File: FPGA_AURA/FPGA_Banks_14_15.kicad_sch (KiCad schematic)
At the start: 15 parts, among them U1 XC7A35T-2FTG256C

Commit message: DDR3 Routing closed!
Finally DDR3 has been routed, verified, and length matched. Further validation still required.
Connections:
- net DDR3_A0: now also U1.D10 (IO_0_15); no longer U1.B11 (IO_L4N_T0_15)
- net DDR3_A1: now also U1.C14 (IO_L8P_T1_AD10P_15); no longer U1.B16 (IO_L10N_T1_AD11N_15)
- net DDR3_A10: now also U1.C12 (IO_L11N_T1_SRCC_15); no longer U1.A14 (IO_L7N_T1_AD2N_15)
- net DDR3_A12: now also U1.C13 (IO_L12N_T1_MRCC_15); no longer U1.A15 (IO_L9N_T1_DQS_AD3N_15)
- net DDR3_A13: now also U1.B10 (IO_L4P_T0_15); no longer U1.D10 (IO_0_15)
- net DDR3_A2: now also U1.D13 (IO_L12P_T1_MRCC_15); no longer U1.C13 (IO_L12N_T1_MRCC_15)
- net DDR3_A3: now also U1.A15 (IO_L9N_T1_DQS_AD3N_15); no longer U1.B12 (IO_L5P_T0_AD9P_15)
- net DDR3_A4: now also U1.A12 (IO_L5N_T0_AD9N_15); no longer U1.B10 (IO_L4P_T0_15)
- net DDR3_A5: now also U1.B15 (IO_L9P_T1_DQS_AD3P_15); no longer U1.D8 (IO_L6P_T0_15)
- net DDR3_A6: now also U1.B11 (IO_L4N_T0_15); no longer U1.C9 (IO_L1N_T0_AD0N_15)
- net DDR3_A7: now also U1.B16 (IO_L10N_T1_AD11N_15); no longer U1.C8 (IO_L1P_T0_AD0P_15)
- net DDR3_A9: now also U1.C16 (IO_L10P_T1_AD11P_15); no longer U1.D9 (IO_L6N_T0_VREF_15)
- net DDR3_BA0: now also U1.B14 (IO_L8N_T1_AD10N_15); no longer U1.C12 (IO_L11N_T1_SRCC_15)
- net DDR3_BA1: now also U1.B12 (IO_L5P_T0_AD9P_15); no longer U1.A12 (IO_L5N_T0_AD9N_15)
- net DDR3_BA2: now also U1.D9 (IO_L6N_T0_VREF_15); no longer U1.A13 (IO_L7P_T1_AD2P_15)
- net DDR3_CAS: now also U1.A13 (IO_L7P_T1_AD2P_15); no longer U1.B14 (IO_L8N_T1_AD10N_15)
- net DDR3_CS: now also U1.A14 (IO_L7N_T1_AD2N_15); no longer U1.B15 (IO_L9P_T1_DQS_AD3P_15)
- net DDR3_ODT: now also U1.C8 (IO_L1P_T0_AD0P_15); no longer U1.C16 (IO_L10P_T1_AD11P_15)
- net DDR3_RAS: now also U1.D8 (IO_L6P_T0_15); no longer U1.C14 (IO_L8P_T1_AD10P_15)
- net DDR3_WE: now also U1.C9 (IO_L1N_T0_AD0N_15); no longer U1.D13 (IO_L12P_T1_MRCC_15)

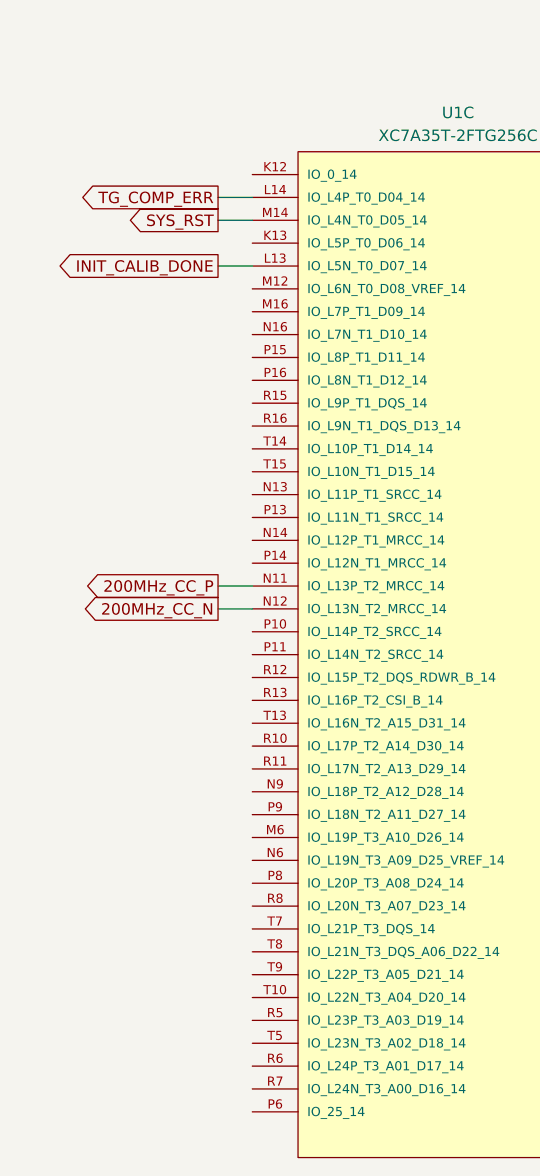
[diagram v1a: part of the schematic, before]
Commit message: Started pinout after successful Vivado bitstream generation.
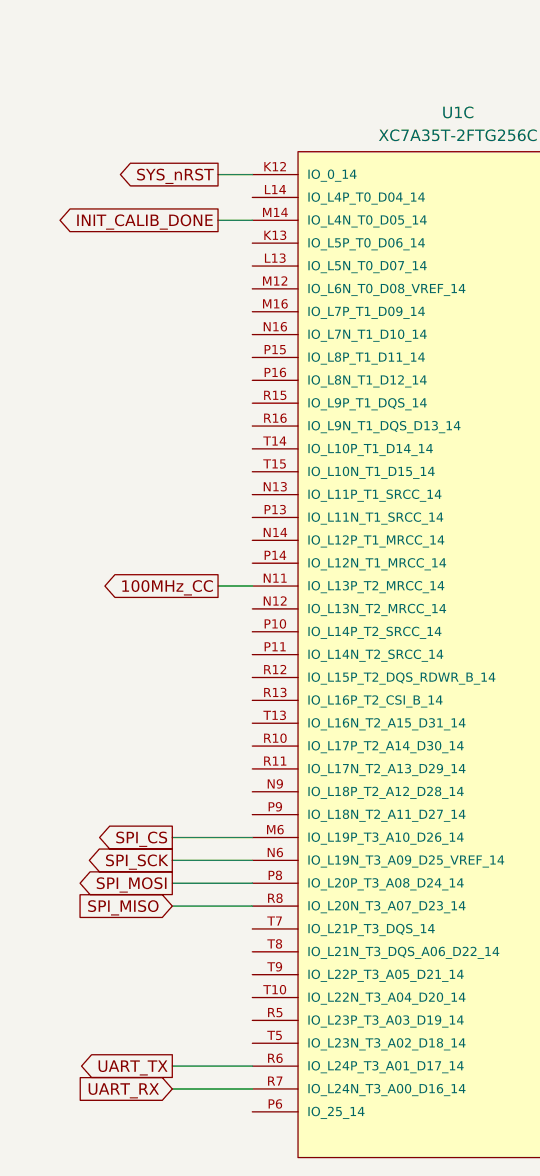
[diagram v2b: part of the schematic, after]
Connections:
- net SYS_RST is gone; now on net INIT_CALIB_DONE: U1.M14 (IO_L4N_T0_D05_14)
- net INIT_CALIB_DONE: no longer U1.L13 (IO_L5N_T0_D07_14)
- net SYS_nRST: now reaches U1.K12 (IO_0_14)
- net SPI_CS: now reaches U1.M6 (IO_L19P_T3_A10_D26_14)
- net SPI_SCK: now reaches U1.N6 (IO_L19N_T3_A09_D25_VREF_14)
- net SPI_MOSI: now reaches U1.P8 (IO_L20P_T3_A08_D24_14)
- net UART_TX: now reaches U1.R6 (IO_L24P_T3_A01_D17_14)
- net UART_RX: now reaches U1.R7 (IO_L24N_T3_A00_D16_14)
- net SPI_MISO: now reaches U1.R8 (IO_L20N_T3_A07_D23_14)
- net 200MHz_CC_N: no longer names the net of U1.N12 (IO_L13N_T2_MRCC_14)
- net 200MHz_CC_P renamed 100MHz_CC
- net TG_COMP_ERR: no longer names the net of U1.L14 (IO_L4P_T0_D04_14)

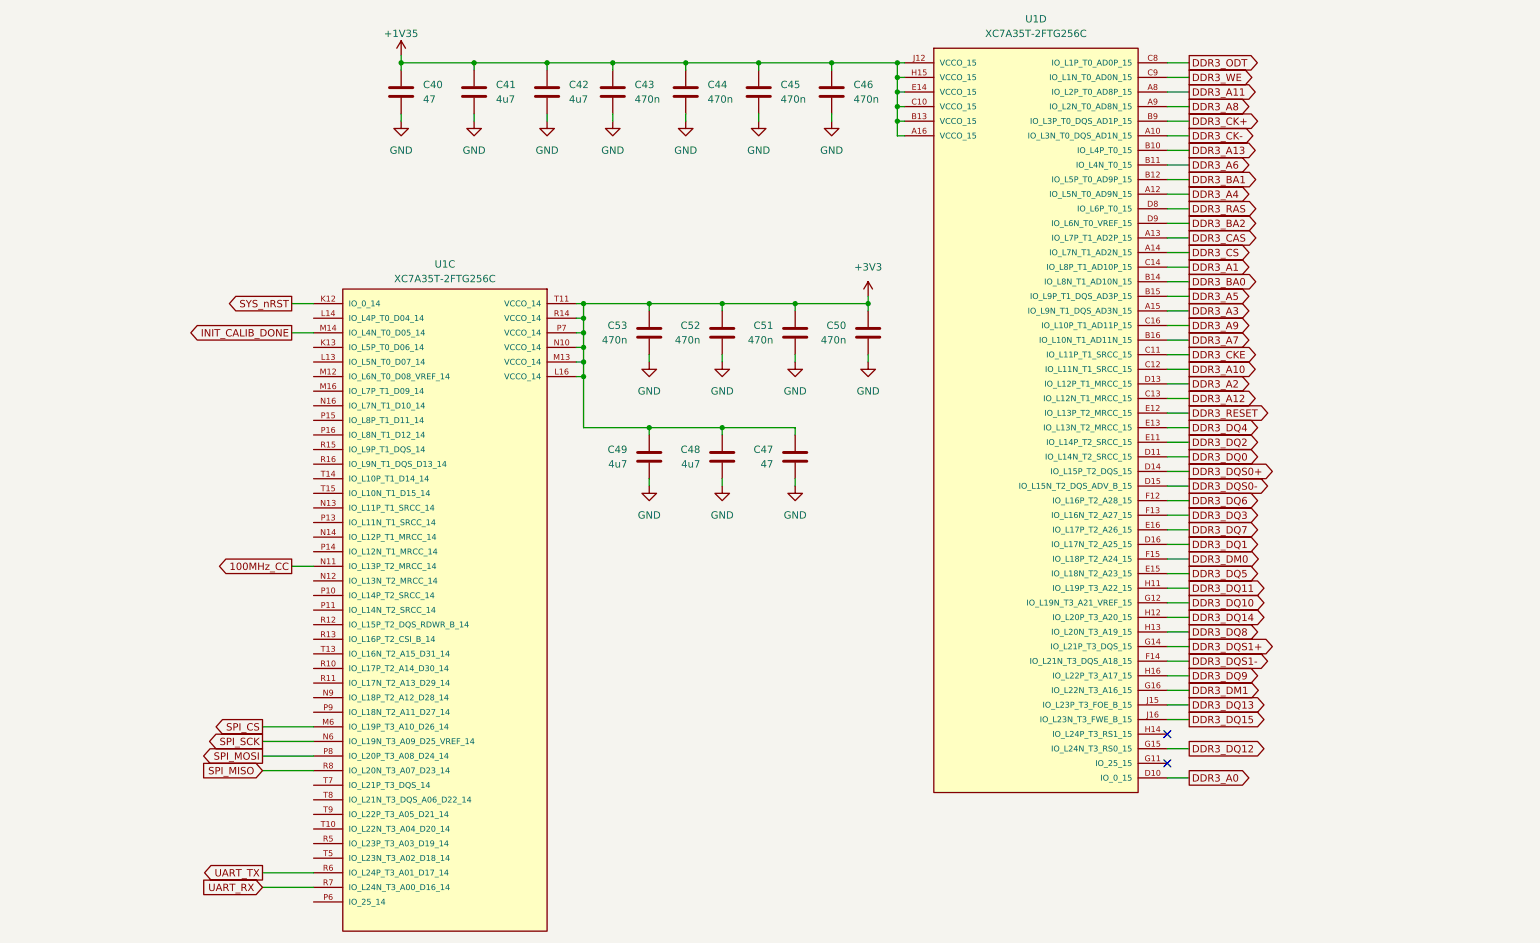
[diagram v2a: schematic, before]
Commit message: Connector pinnout defined loosly. Next is schematic clean-up followed by routing.
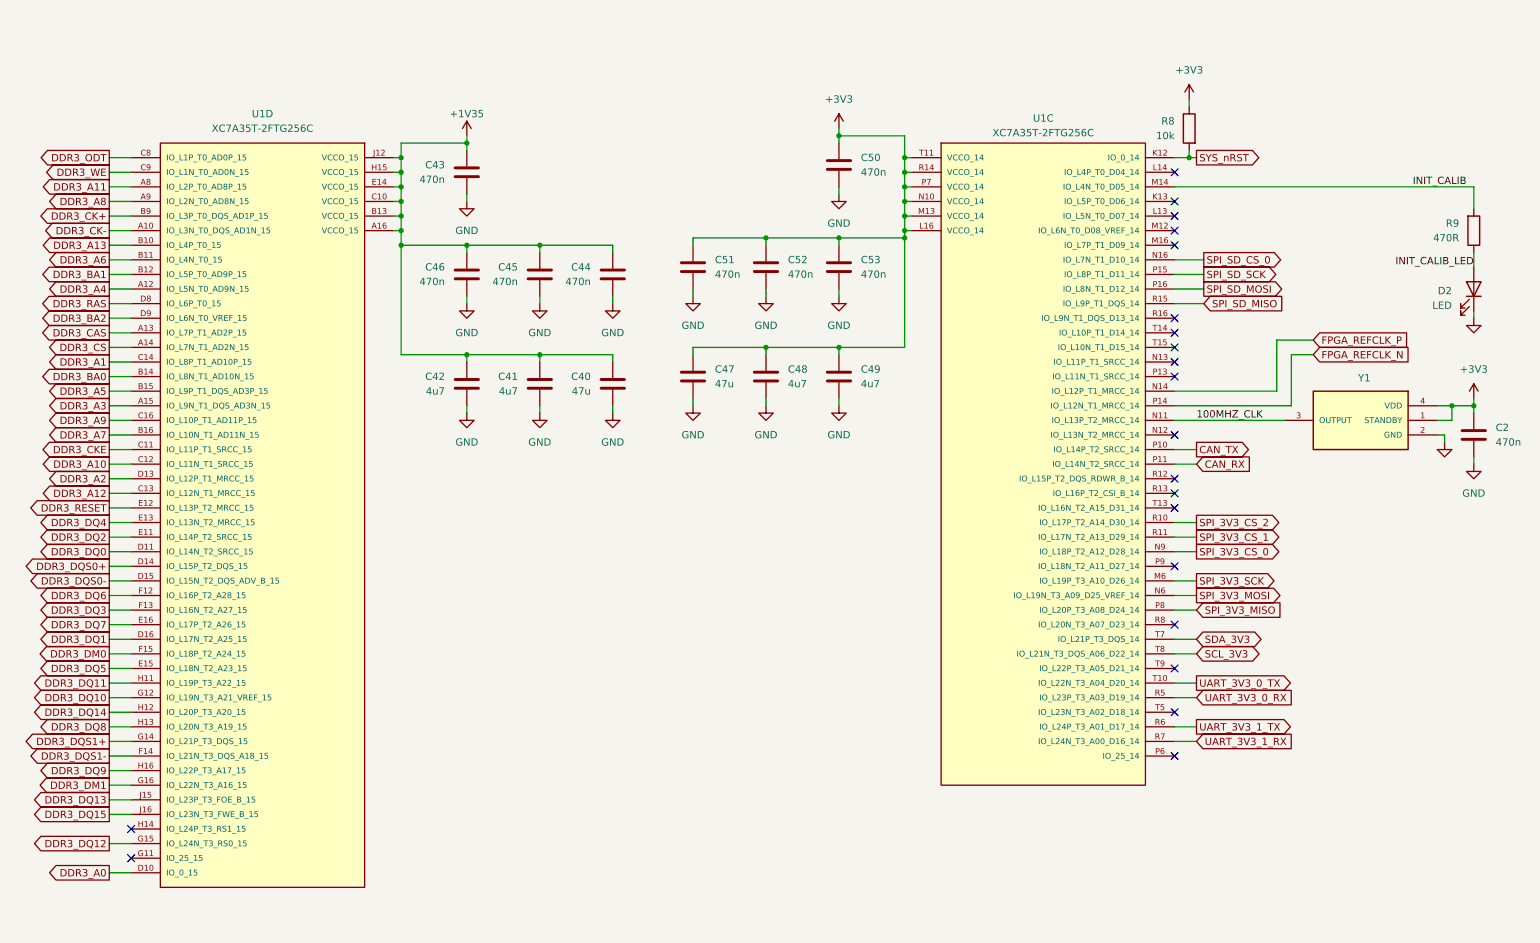
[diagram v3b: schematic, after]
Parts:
- added C2: 470n, Capacitor_SMD:C_0402_1005Metric, symbol Device:C
- added D2: LED, LED_SMD:LED_0603_1608Metric, symbol Device:LED
- added R8: 10k, Resistor_SMD:R_0402_1005Metric, symbol Device:R
- added R9: 470R, Resistor_SMD:R_0402_1005Metric, symbol Device:R
- added Y1: ASEM1-100.000MHZ-LC-T, ASEM1-100.000MHZ-LC-T:XTAL_ASEM1-100.000MHZ-LC-T, symbol ASEM1-100.000MHZ-LC-T:ASEM1-100.000MHZ-LC-T
- C40, C47: value 47 -> 47u
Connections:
- net +3V3: now also C2.1, R8.1, Y1.1 (STANDBY), Y1.4 (VDD)
- net GND: now also C2.2, D2.1 (K), Y1.2 (GND)
- net SYS_nRST: now also R8.2
- net FPGA_REFCLK_P: now reaches U1.N14 (IO_L12P_T1_MRCC_14)
- net SPI_SD_CS_0: now reaches U1.N16 (IO_L7N_T1_D10_14)
- net SPI_3V3_CS_0: now reaches U1.N9 (IO_L18P_T2_A12_D28_14)
- net CAN_TX: now reaches U1.P10 (IO_L14P_T2_SRCC_14)
- net CAN_RX: now reaches U1.P11 (IO_L14N_T2_SRCC_14)
- net FPGA_REFCLK_N: now reaches U1.P14 (IO_L12N_T1_MRCC_14)
- net SPI_SD_SCK: now reaches U1.P15 (IO_L8P_T1_D11_14)
- net SPI_SD_MOSI: now reaches U1.P16 (IO_L8N_T1_D12_14)
- net SPI_3V3_CS_2: now reaches U1.R10 (IO_L17P_T2_A14_D30_14)
- net SPI_3V3_CS_1: now reaches U1.R11 (IO_L17N_T2_A13_D29_14)
- net SPI_SD_MISO: now reaches U1.R15 (IO_L9P_T1_DQS_14)
- net UART_3V3_0_RX: now reaches U1.R5 (IO_L23P_T3_A03_D19_14)
- net UART_3V3_0_TX: now reaches U1.T10 (IO_L22N_T3_A04_D20_14)
- net SDA_3V3: now reaches U1.T7 (IO_L21P_T3_DQS_14)
- net SCL_3V3: now reaches U1.T8 (IO_L21N_T3_DQS_A06_D22_14)
- net 100MHz_CC renamed 100MHZ_CLK
- net 100MHZ_CLK: now also Y1.3 (OUTPUT)
- net INIT_CALIB_DONE renamed INIT_CALIB
- net INIT_CALIB: now also R9.2
- net SPI_CS renamed SPI_3V3_SCK
- net SPI_MISO: no longer names the net of U1.R8 (IO_L20N_T3_A07_D23_14)
- net SPI_MOSI renamed SPI_3V3_MISO
- net SPI_SCK renamed SPI_3V3_MOSI
- net UART_RX renamed UART_3V3_1_RX
- net UART_TX renamed UART_3V3_1_TX
- new net INIT_CALIB_LED: D2.2 (A), R9.1
- no-connect marks 2 -> 21
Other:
- moved on the sheet: C40, C41, C42, C43, C44, C45, C46, C47, C48, C49, C50, C51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

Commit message: Finished schematic to start routing again, and started MII fanout from connector.
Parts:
- added D501: LED, LED_SMD:LED_0603_1608Metric, symbol Device:LED
- added R502: 470R, Resistor_SMD:R_0402_1005Metric, symbol Device:R
- renumbered C43 to C500, C46 to C501, C45 to C502, C44 to C503, C42 to C504, C41 to C505, C40 to C506, C50 to C507, C51 to C508, C52 to C509, C53 to C510, C47 to C511, C48 to C512, C49 to C513, C2 to C514, D2 to D500, R8 to R500, R9 to R501, Y1 to Y500
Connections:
- net GND: now also D501.1 (K)
- net GPIO: now reaches U1.K13 (IO_L5P_T0_D06_14)
- net GPIO: now also R502.2
- new net GPIO_LED: D501.2 (A), R502.1
- no-connect marks 21 -> 20
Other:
- company: (none) -> Alexander Armitage
- title: (none) -> XC7A35T Banks 14, 15

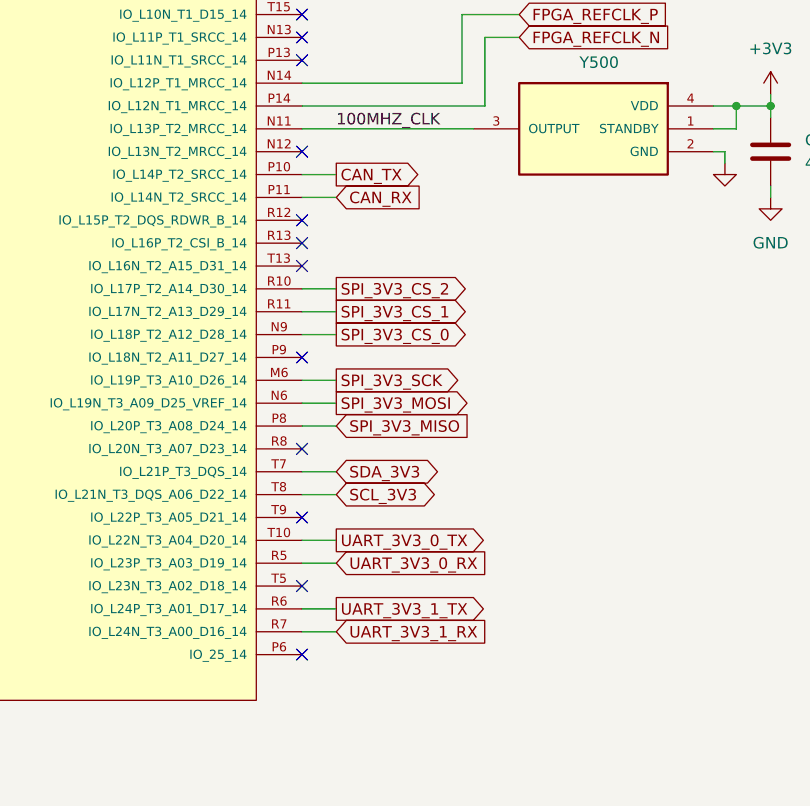
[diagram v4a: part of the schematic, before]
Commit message: Power planes done on layers 3 and 4 as well as almost all mezzanine connections made. QSPI and misc left to do.
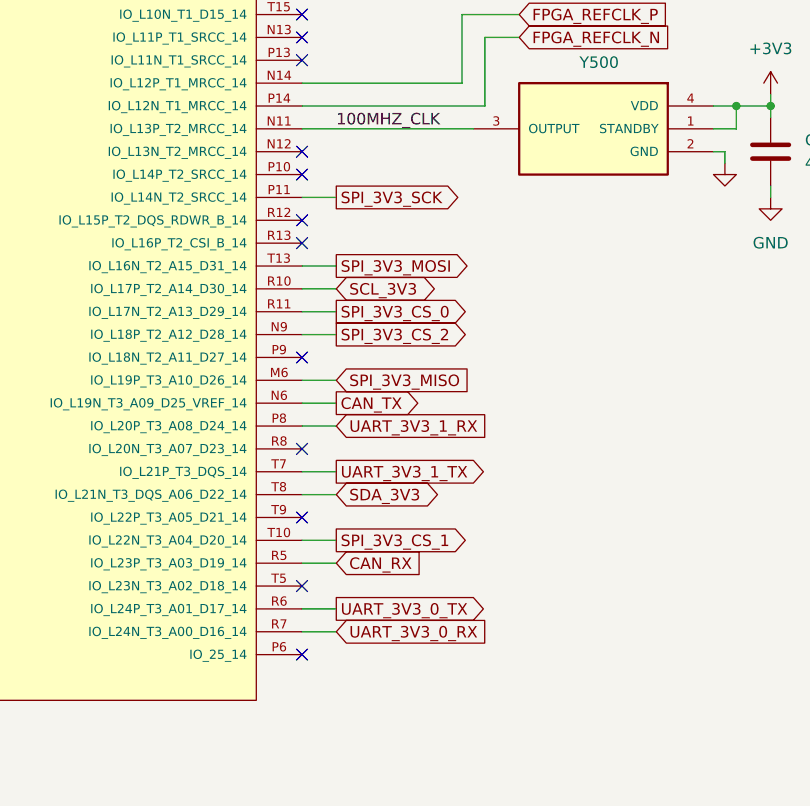
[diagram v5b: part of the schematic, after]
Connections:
- net CAN_RX: now also U1.R5 (IO_L23P_T3_A03_D19_14); no longer U1.P11 (IO_L14N_T2_SRCC_14)
- net CAN_TX: now also U1.N6 (IO_L19N_T3_A09_D25_VREF_14); no longer U1.P10 (IO_L14P_T2_SRCC_14)
- net SCL_3V3: now also U1.R10 (IO_L17P_T2_A14_D30_14); no longer U1.T8 (IO_L21N_T3_DQS_A06_D22_14)
- net SDA_3V3: now also U1.T8 (IO_L21N_T3_DQS_A06_D22_14); no longer U1.T7 (IO_L21P_T3_DQS_14)
- net SPI_3V3_CS_0: now also U1.R11 (IO_L17N_T2_A13_D29_14); no longer U1.N9 (IO_L18P_T2_A12_D28_14)
- net SPI_3V3_CS_1: now also U1.T10 (IO_L22N_T3_A04_D20_14); no longer U1.R11 (IO_L17N_T2_A13_D29_14)
- net SPI_3V3_CS_2: now also U1.N9 (IO_L18P_T2_A12_D28_14); no longer U1.R10 (IO_L17P_T2_A14_D30_14)
- net SPI_3V3_MISO: now also U1.M6 (IO_L19P_T3_A10_D26_14); no longer U1.P8 (IO_L20P_T3_A08_D24_14)
- net SPI_3V3_MOSI: now also U1.T13 (IO_L16N_T2_A15_D31_14); no longer U1.N6 (IO_L19N_T3_A09_D25_VREF_14)
- net SPI_3V3_SCK: now also U1.P11 (IO_L14N_T2_SRCC_14); no longer U1.M6 (IO_L19P_T3_A10_D26_14)
- net UART_3V3_0_RX: now also U1.R7 (IO_L24N_T3_A00_D16_14); no longer U1.R5 (IO_L23P_T3_A03_D19_14)
- net UART_3V3_0_TX: now also U1.R6 (IO_L24P_T3_A01_D17_14); no longer U1.T10 (IO_L22N_T3_A04_D20_14)
- net UART_3V3_1_RX: now also U1.P8 (IO_L20P_T3_A08_D24_14); no longer U1.R7 (IO_L24N_T3_A00_D16_14)
- net UART_3V3_1_TX: now also U1.T7 (IO_L21P_T3_DQS_14); no longer U1.R6 (IO_L24P_T3_A01_D17_14)
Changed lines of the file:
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@@
 	)
 	(no_connect
-		(at 222.25 106.68)
-	)
-	(no_connect
 		(at 222.25 48.26)
 	)
@@
 		(at 222.25 149.86)
 	)
+	(no_connect
+		(at 222.25 96.52)
+	)
 	(wire
 		(pts
@@
 	(wire
 		(pts
+			(xy 222.25 106.68) (xy 226.06 106.68)
+		)
+		(stroke
+			(width 0)
+			(type default)
+		)
+	)
+	(wire
+		(pts
 			(xy 163.83 41.91) (xy 163.83 43.18)
 		)
@@
 	(wire
 		(pts
-			(xy 226.06 96.52) (xy 222.25 96.52)
-		)
-		(stroke
-			(width 0)
-			(type default)
-		)
-	)
-	(wire
-		(pts
 			(xy 40.64 86.36) (xy 36.83 86.36)
 		)
@@
 	(global_label "SDA_3V3"
 		(shape bidirectional)
-		(at 226.06 129.54 0)
+		(at 226.06 132.08 0)
 		(fields_autoplaced yes)
 		(effects
@@
 		)
 		(property "Intersheetrefs" "${INTERSHEET_REFS}"
-			(at 238.1998 129.54 0)
+			(at 238.1998 132.08 0)
 			(hide yes)
 			(show_name no)
@@
 	(global_label "SPI_3V3_SCK"
 		(shape output)
-		(at 226.06 119.38 0)
+		(at 226.06 99.06 0)
 		(fields_autoplaced yes)
 		(effects
@@
 		)
 		(property "Intersheetrefs" "${INTERSHEET_REFS}"
-			(at 241.3218 119.38 0)
+			(at 241.3218 99.06 0)
 			(hide yes)
 			(show_name no)
@@
 	(global_label "UART_3V3_0_TX"
 		(shape output)
-		(at 226.06 137.16 0)
+		(at 226.06 144.78 0)
 		(fields_autoplaced yes)
 		(effects
@@
 		)
 		(property "Intersheetrefs" "${INTERSHEET_REFS}"
-			(at 243.4989 137.16 0)
+			(at 243.4989 144.78 0)
 			(hide yes)
 			(show_name no)
@@
 	(global_label "SPI_3V3_MISO"
 		(shape input)
-		(at 226.06 124.46 0)
+		(at 226.06 119.38 0)
 		(fields_autoplaced yes)
 		(effects
@@
 		)
 		(property "Intersheetrefs" "${INTERSHEET_REFS}"
-			(at 242.1685 124.46 0)
+			(at 242.1685 119.38 0)
 			(hide yes)
 			(show_name no)
@@
 	(global_label "UART_3V3_0_RX"
 		(shape input)
-		(at 226.06 139.7 0)
+		(at 226.06 147.32 0)
 		(fields_autoplaced yes)
 		(effects
@@
 		)
 		(property "Intersheetrefs" "${INTERSHEET_REFS}"
-			(at 243.8013 139.7 0)
+			(at 243.8013 147.32 0)
 			(hide yes)
 			(show_name no)
@@
 	(global_label "SPI_3V3_CS_0"
 		(shape output)
-		(at 226.06 114.3 0)
+		(at 226.06 111.76 0)
 		(fields_autoplaced yes)
 		(effects
@@
 		)
 		(property "Intersheetrefs" "${INTERSHEET_REFS}"
-			(at 242.2289 114.3 0)
+			(at 242.2289 111.76 0)
 			(hide yes)
 			(show_name no)
@@
 	(global_label "SCL_3V3"
 		(shape bidirectional)
-		(at 226.06 132.08 0)
+		(at 226.06 109.22 0)
 		(fields_autoplaced yes)
 		(effects
@@
 		)
 		(property "Intersheetrefs" "${INTERSHEET_REFS}"
-			(at 238.1393 132.08 0)
+			(at 238.1393 109.22 0)
 			(hide yes)
 			(show_name no)
@@
 	(global_label "SPI_3V3_MOSI"
 		(shape output)
-		(at 226.06 121.92 0)
+		(at 226.06 106.68 0)
 		(fields_autoplaced yes)
 		(effects
@@
 		)
 		(property "Intersheetrefs" "${INTERSHEET_REFS}"
-			(at 242.1685 121.92 0)
+			(at 242.1685 106.68 0)
 			(hide yes)
 			(show_name no)
@@
 	(global_label "UART_3V3_1_TX"
 		(shape output)
-		(at 226.06 144.78 0)
+		(at 226.06 129.54 0)
 		(fields_autoplaced yes)
 		(effects
@@
 		)
 		(property "Intersheetrefs" "${INTERSHEET_REFS}"
-			(at 243.4989 144.78 0)
+			(at 243.4989 129.54 0)
 			(hide yes)
 			(show_name no)
@@
 	(global_label "CAN_RX"
 		(shape input)
-		(at 226.06 99.06 0)
+		(at 226.06 139.7 0)
 		(fields_autoplaced yes)
 		(effects
@@
 		)
 		(property "Intersheetrefs" "${INTERSHEET_REFS}"
-			(at 236.1814 99.06 0)
+			(at 236.1814 139.7 0)
 			(hide yes)
 			(show_name no)
@@
 	(global_label "SPI_3V3_CS_1"
 		(shape output)
-		(at 226.06 111.76 0)
+		(at 226.06 137.16 0)
 		(fields_autoplaced yes)
 		(effects
@@
 		)
 		(property "Intersheetrefs" "${INTERSHEET_REFS}"
-			(at 242.2289 111.76 0)
+			(at 242.2289 137.16 0)
 			(hide yes)
 			(show_name no)
@@
 	(global_label "SPI_3V3_CS_2"
 		(shape output)
-		(at 226.06 109.22 0)
+		(at 226.06 114.3 0)
 		(fields_autoplaced yes)
 		(effects
@@
 		)
 		(property "Intersheetrefs" "${INTERSHEET_REFS}"
-			(at 242.2289 109.22 0)
+			(at 242.2289 114.3 0)
 			(hide yes)
 			(show_name no)
@@
 	(global_label "CAN_TX"
 		(shape output)
-		(at 226.06 96.52 0)
+		(at 226.06 121.92 0)
 		(fields_autoplaced yes)
 		(effects
@@
 		)
 		(property "Intersheetrefs" "${INTERSHEET_REFS}"
-			(at 235.879 96.52 0)
+			(at 235.879 121.92 0)
 			(hide yes)
 			(show_name no)
@@
 	(global_label "UART_3V3_1_RX"
 		(shape input)
-		(at 226.06 147.32 0)
+		(at 226.06 124.46 0)
 		(fields_autoplaced yes)
 		(effects
@@
 		)
 		(property "Intersheetrefs" "${INTERSHEET_REFS}"
-			(at 243.8013 147.32 0)
+			(at 243.8013 124.46 0)
 			(hide yes)
 			(show_name no)
